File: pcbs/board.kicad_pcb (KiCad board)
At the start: 2 copper layers, 169.9 x 163.3 mm, 89 parts

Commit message: Tweaked mount points to avoid any switch overlap
Mounts near the offset columns were close to overlapping adjacent
switches
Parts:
- moved MH5 47.0 mm to (135.5, 129.5)
- moved MH2 23.6 mm to (135.5, 34.5)
- moved MH6 19.6 mm to (97.5, 129.5)
- moved MH3 4.76 mm to (173.5, 58.5)
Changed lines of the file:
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@@
   (footprint "ceoloide:mounting_hole_npth"
     (layer "F.Cu")
-    (at 116.525 48.525 0)
+    (at 135.525 34.475 0)
     (property "Reference" "MH2"
       (at 0 2.55 0)
@@
   (footprint "ceoloide:mounting_hole_npth"
     (layer "F.Cu")
-    (at 178.2875 58.525 0)
+    (at 173.525 58.525 0)
     (property "Reference" "MH3"
       (at 0 2.55 0)
@@
   (footprint "ceoloide:mounting_hole_npth"
     (layer "F.Cu")
-    (at 116.525 86.525 0)
+    (at 135.525 129.525 0)
     (property "Reference" "MH5"
       (at 0 2.55 0)
@@
   (footprint "ceoloide:mounting_hole_npth"
     (layer "F.Cu")
-    (at 116.525 124.525 0)
+    (at 97.525 129.525 0)
     (property "Reference" "MH6"
       (at 0 2.55 0)

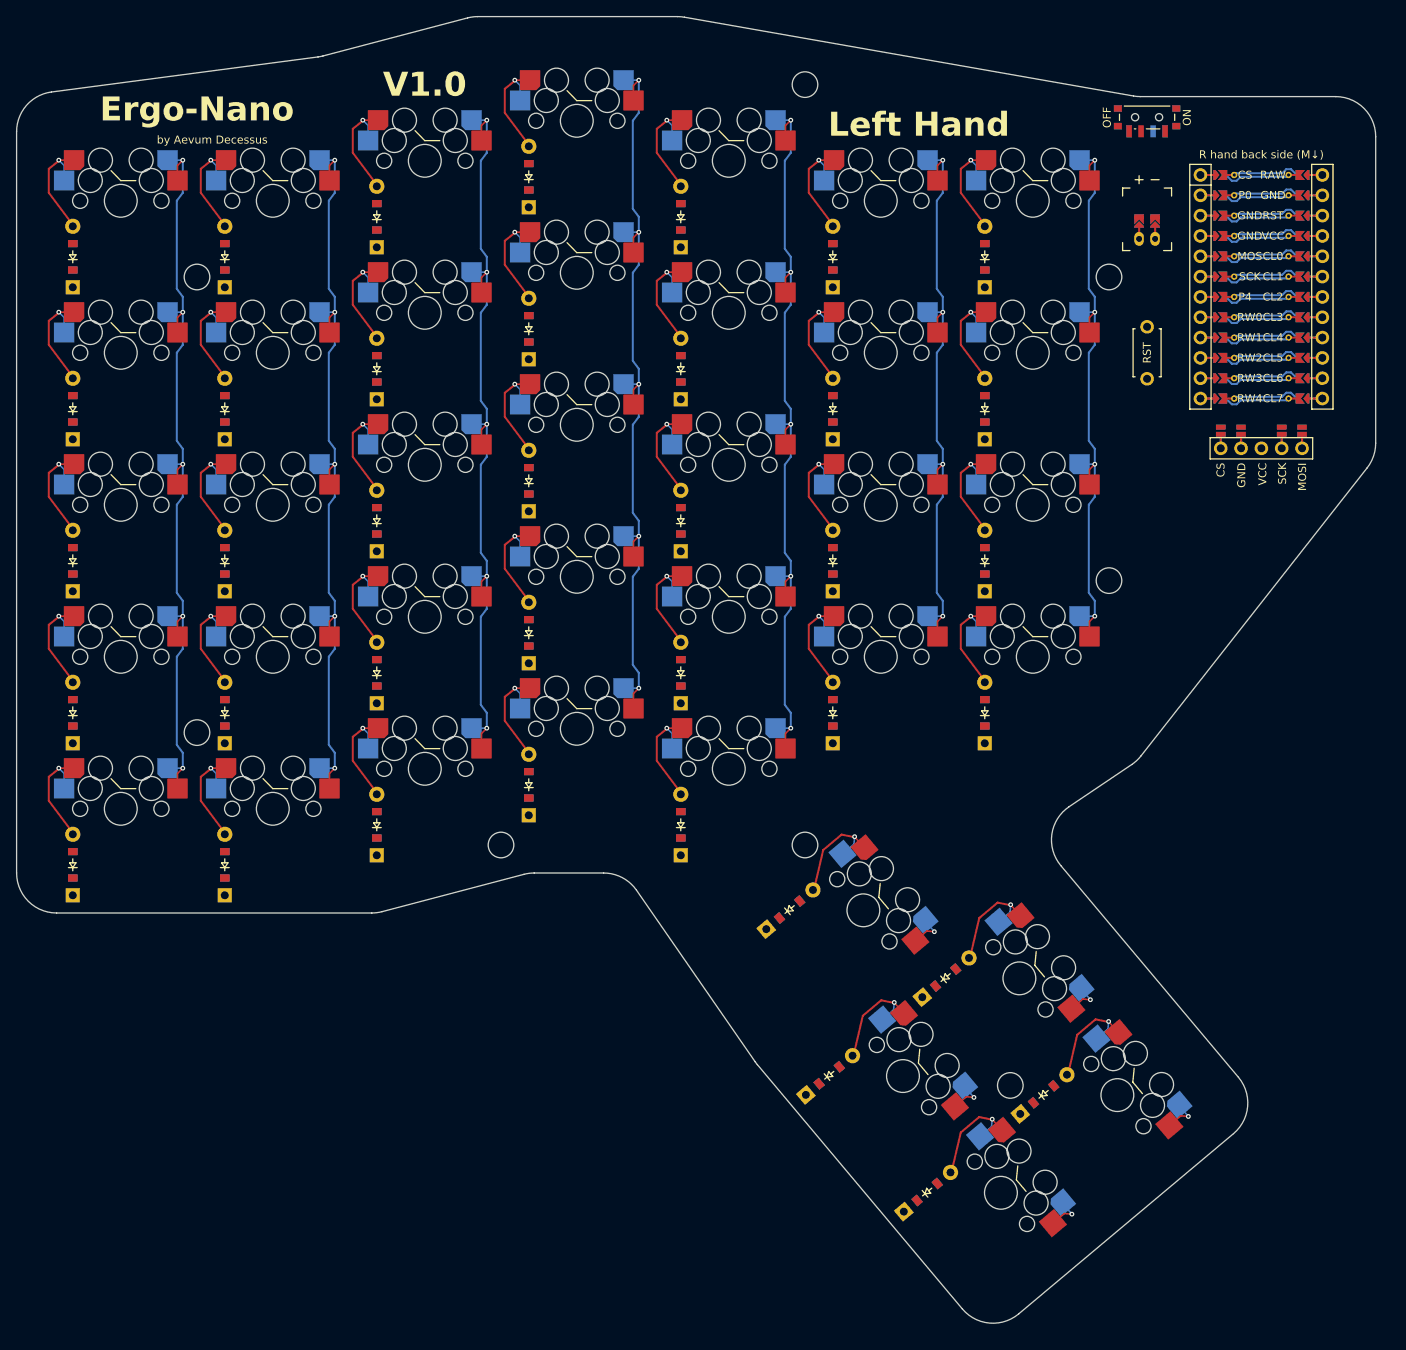
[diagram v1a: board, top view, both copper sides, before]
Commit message: Parameterized more of the layout and subdivided
MCU has a proper outline now that combines with the key outline for the
PCB/case

Switch plate only uses the key outlines for sizing now
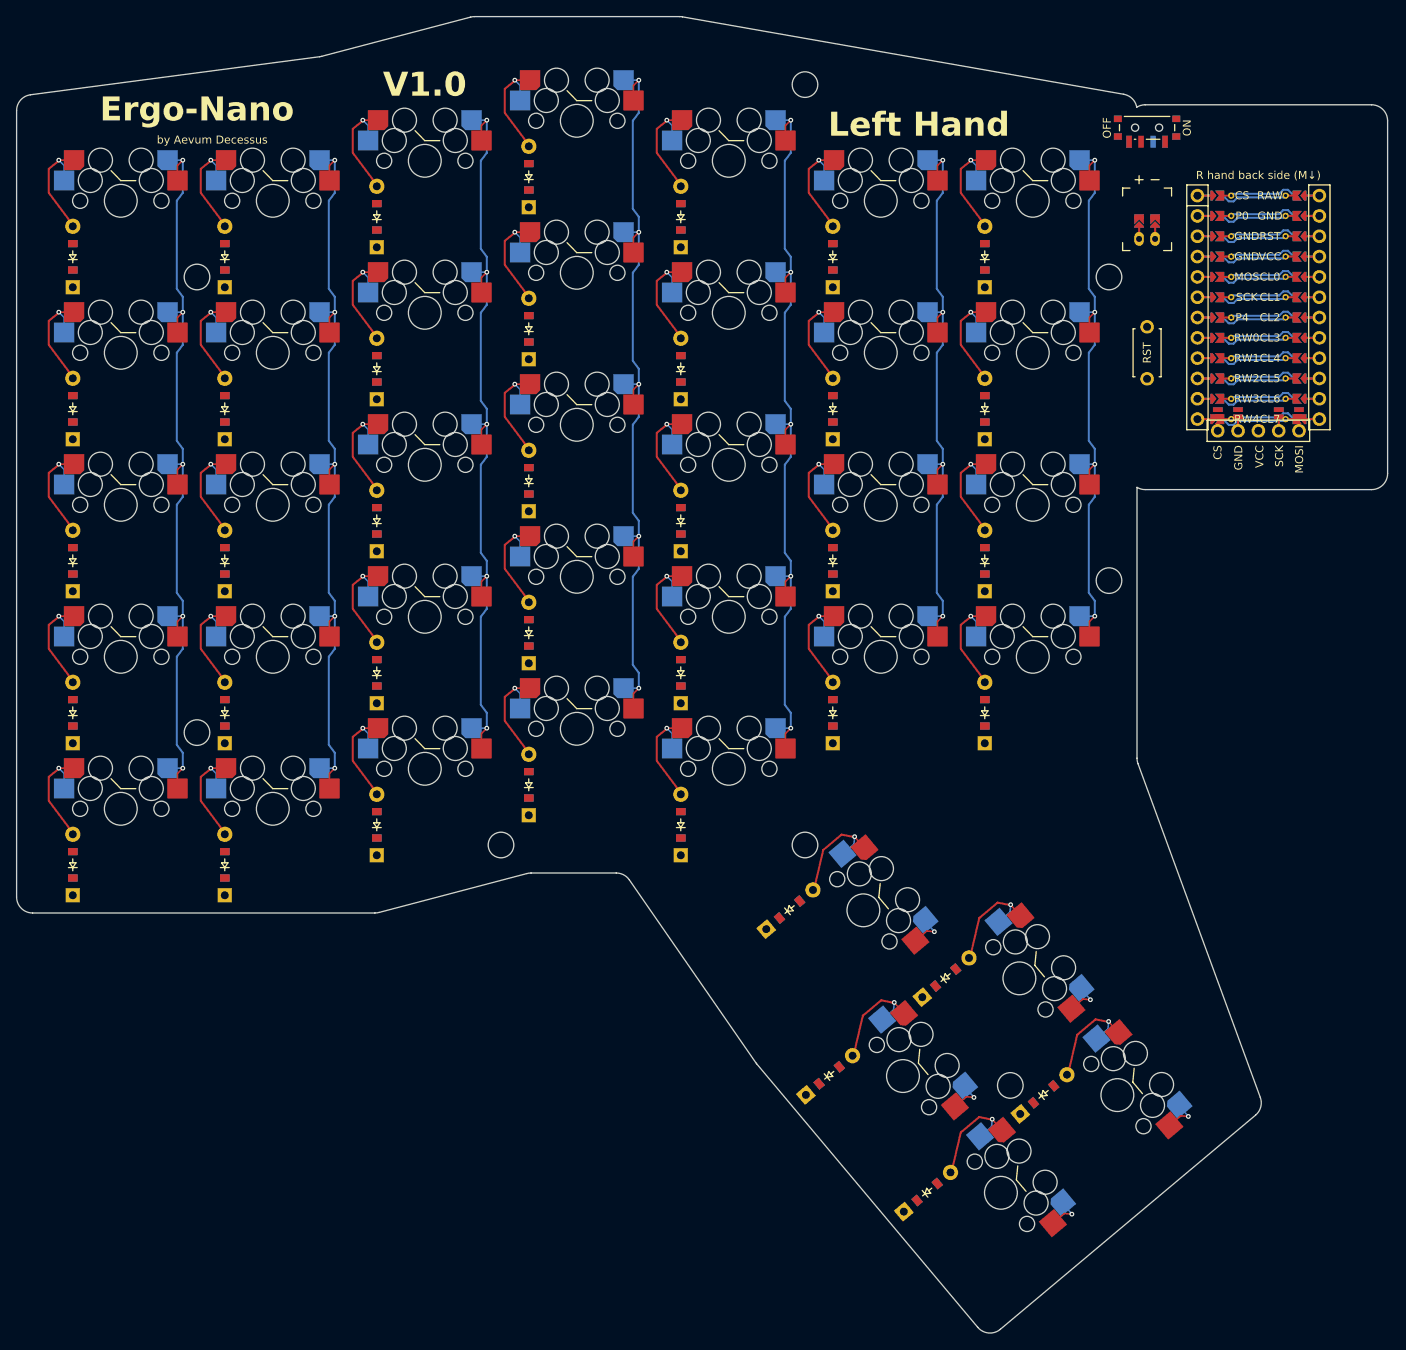
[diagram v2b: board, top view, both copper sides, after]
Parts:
- moved MCU1 2.60 mm to (192.2, 61.0)
- moved DISP1 2.22 mm to (192.2, 61.0)
- moved PWR1 1.30 mm to (178.3, 39.9)
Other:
- board size 169.9 x 163.3 mm -> 171.4 x 164.6 mm

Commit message: Added more meta tags, minor shifts of case/pcb design
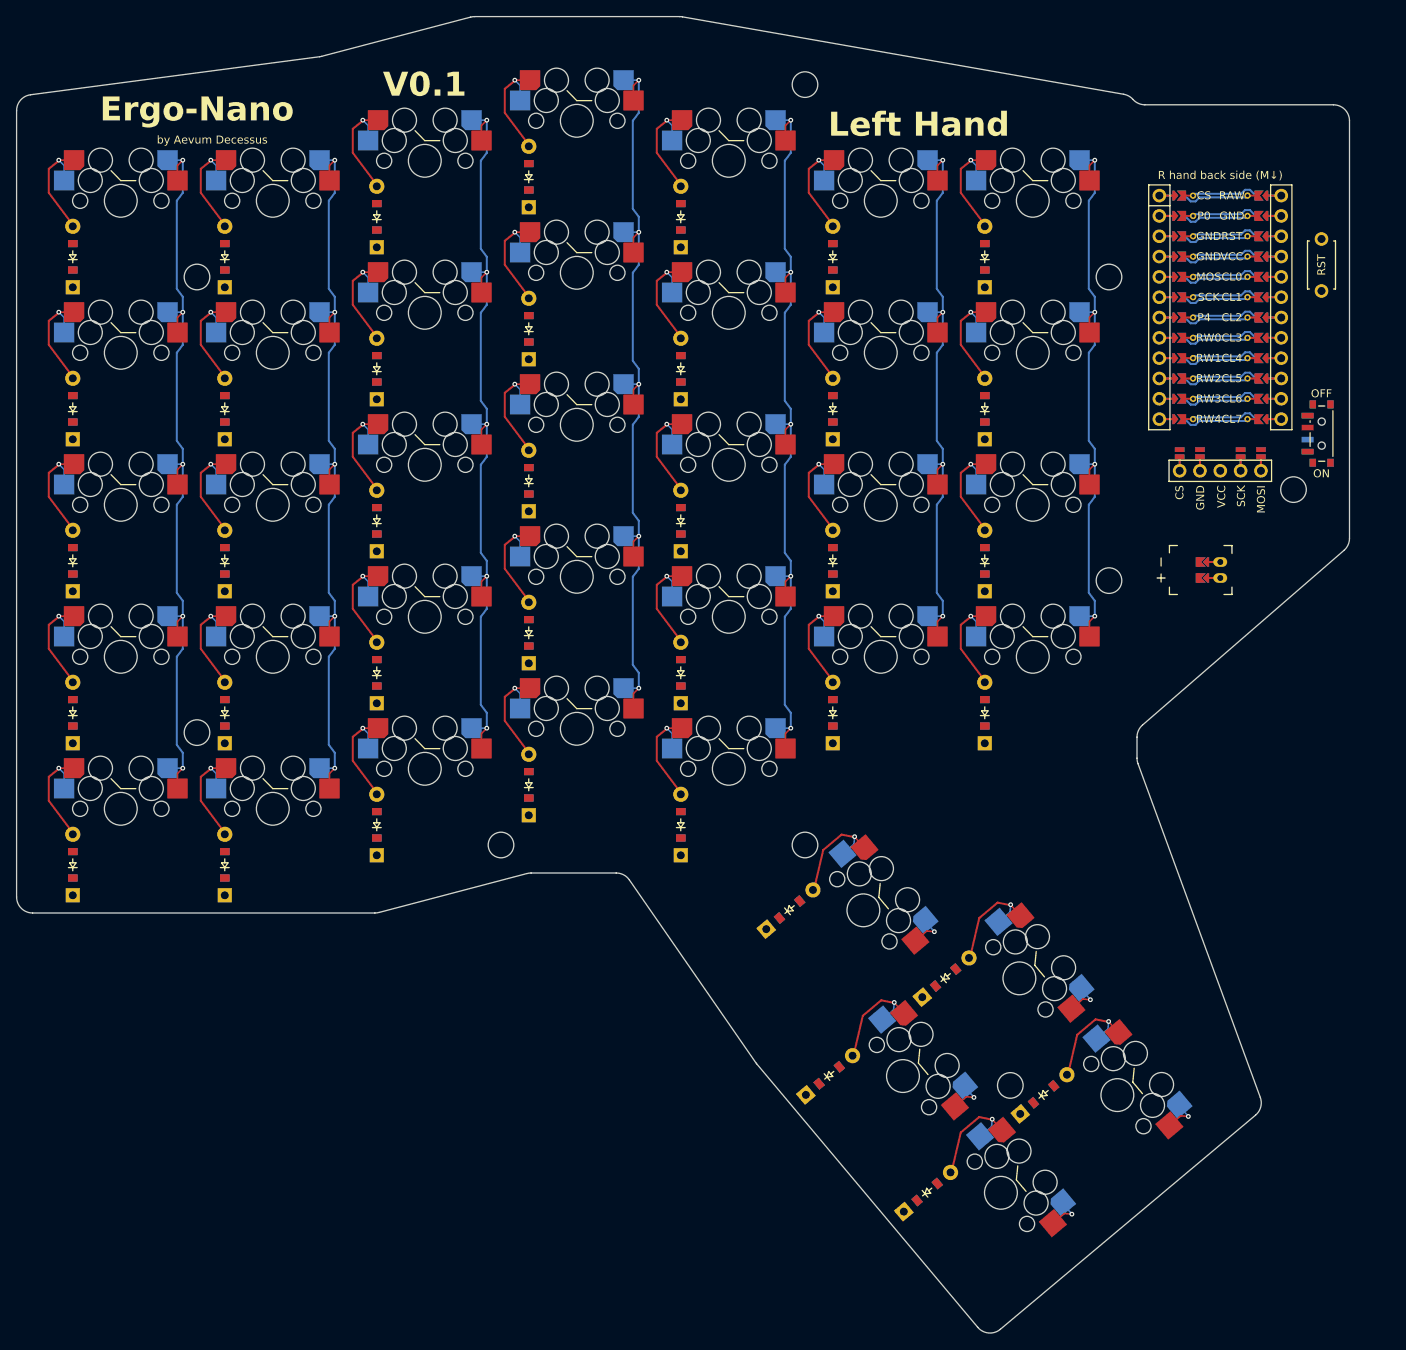
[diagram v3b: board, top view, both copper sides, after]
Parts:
- added MH9: , ceoloide:mounting_hole_npth, F.Cu at (196.6, 85.1)
- moved PWR1 44.0 mm to (200.1, 78.1), turned to 0 degrees
- moved JST1 42.4 mm to (187.4, 95.1), turned to -90 degrees
- moved RST1 24.4 mm to (200.1, 57.0)
- moved DISP1 6.91 mm to (187.4, 66.0)
- moved MCU1 4.76 mm to (187.4, 61.0)
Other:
- board size 171.4 x 164.6 mm -> 166.6 x 164.6 mm
- board text added: "V0.1"
- board text removed: "V1.0"

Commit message: Added many documentation comments, some additions
Now has 3 cases, one for just a bottom plate, one with walls up to the
PCB height, one with walls up to the top of the switch plate.

Actually put the screw head size around each mounting hold, moved the
diodes and traces slightly to adjust
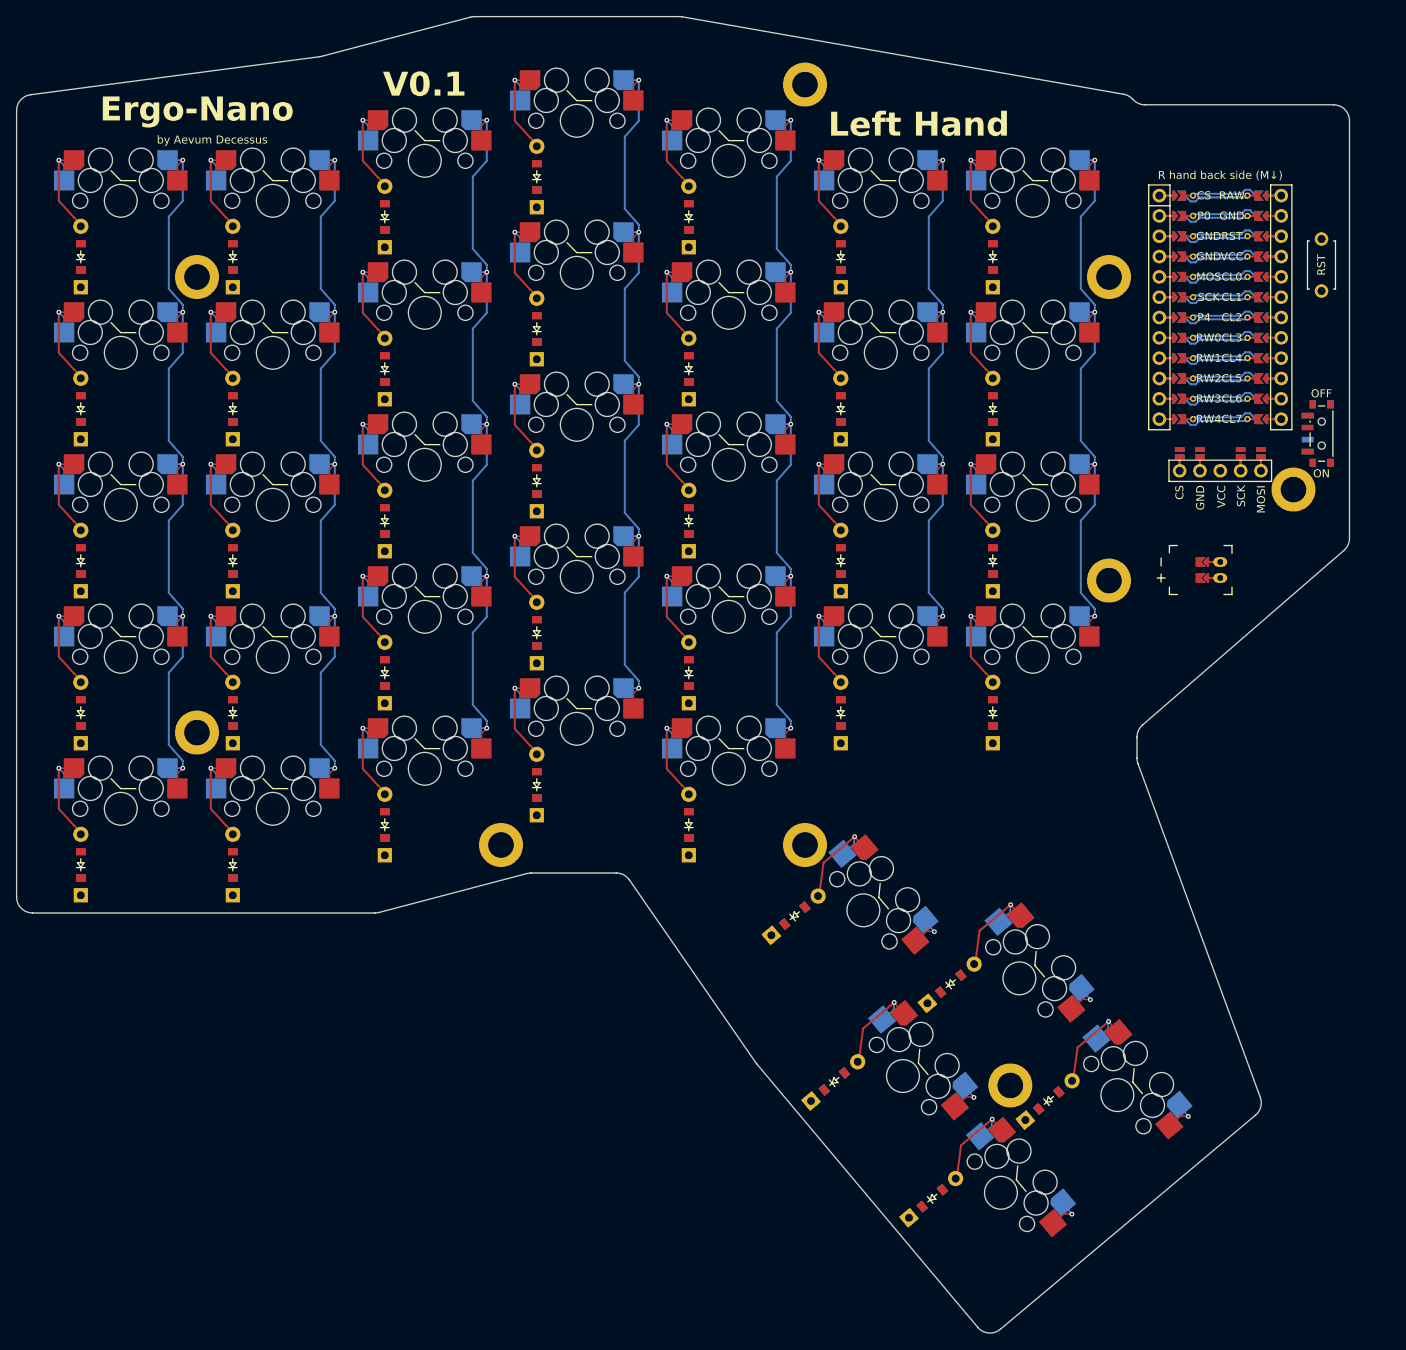
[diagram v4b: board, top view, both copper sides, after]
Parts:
- moved D34 1.00 mm to (134.2, 138.4)
- moved D35 1.00 mm to (139.2, 159.1)
- moved D36 1.00 mm to (153.7, 146.9)
- moved D37 1.00 mm to (151.4, 173.7)
- moved D38 1.00 mm to (166.0, 161.5)
- moved D1 1.00 mm to (45.0, 132.0)
- moved D10 1.00 mm to (64.0, 56.0)
- moved D11 1.00 mm to (83.0, 127.0)
- moved D12 1.00 mm to (83.0, 108.0)
- moved D13 1.00 mm to (83.0, 89.0)
- moved D14 1.00 mm to (83.0, 70.0)
- moved D15 1.00 mm to (83.0, 51.0)
- moved D16 1.00 mm to (102.0, 122.0)
- moved D17 1.00 mm to (102.0, 103.0)
- moved D18 1.00 mm to (102.0, 84.0)
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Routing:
- net (no net): track 852.4 -> 873.6 mm
- net ring_top: track 14.3 -> 13.8 mm
- net ring_num: track 14.3 -> 13.8 mm
- net ring_mod: track 14.3 -> 13.8 mm
- net ring_home: track 14.3 -> 13.8 mm
- net ring_bottom: track 14.3 -> 13.8 mm
- net pinky_top: track 14.3 -> 13.8 mm
- net pinky_num: track 14.3 -> 13.8 mm
- net pinky_mod: track 14.3 -> 13.8 mm
- net pinky_home: track 14.3 -> 13.8 mm
- net pinky_bottom: track 14.3 -> 13.8 mm
- net outer_top: track 14.3 -> 13.8 mm
- net outer_num: track 14.3 -> 13.8 mm
- net outer_mod: track 14.3 -> 13.8 mm
- net outer_home: track 14.3 -> 13.8 mm
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
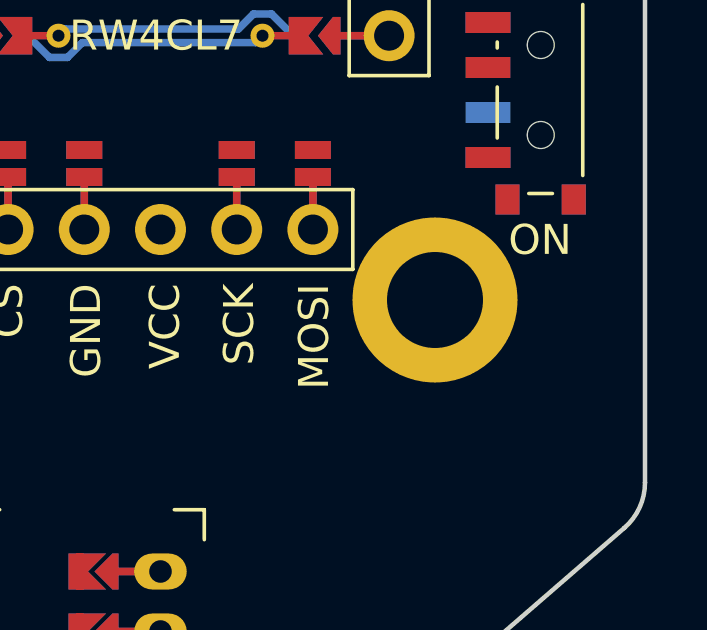
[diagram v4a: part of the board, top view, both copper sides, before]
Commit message: Moved the screw to the bottom right of the MCU
Was overlapping the display slightly
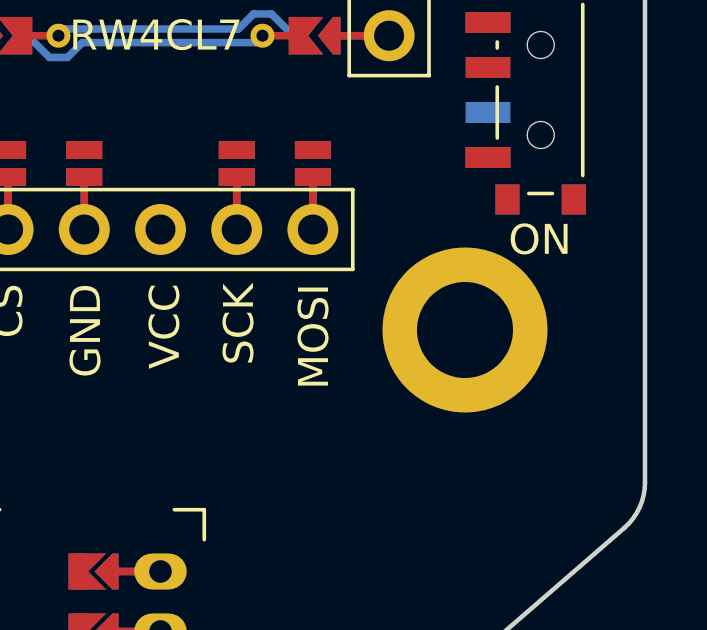
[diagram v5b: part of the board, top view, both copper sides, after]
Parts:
- moved MH9 1.41 mm to (197.6, 86.1)
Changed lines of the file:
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@@
   (footprint "ceoloide:mounting_hole_npth"
     (layer "F.Cu")
-    (at 196.5875 85.1 0)
+    (at 197.5875 86.1 0)
     (property "Reference" "MH9"
       (at 0 2.55 0)
